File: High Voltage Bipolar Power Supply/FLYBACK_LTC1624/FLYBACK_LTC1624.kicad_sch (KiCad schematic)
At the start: 0 parts

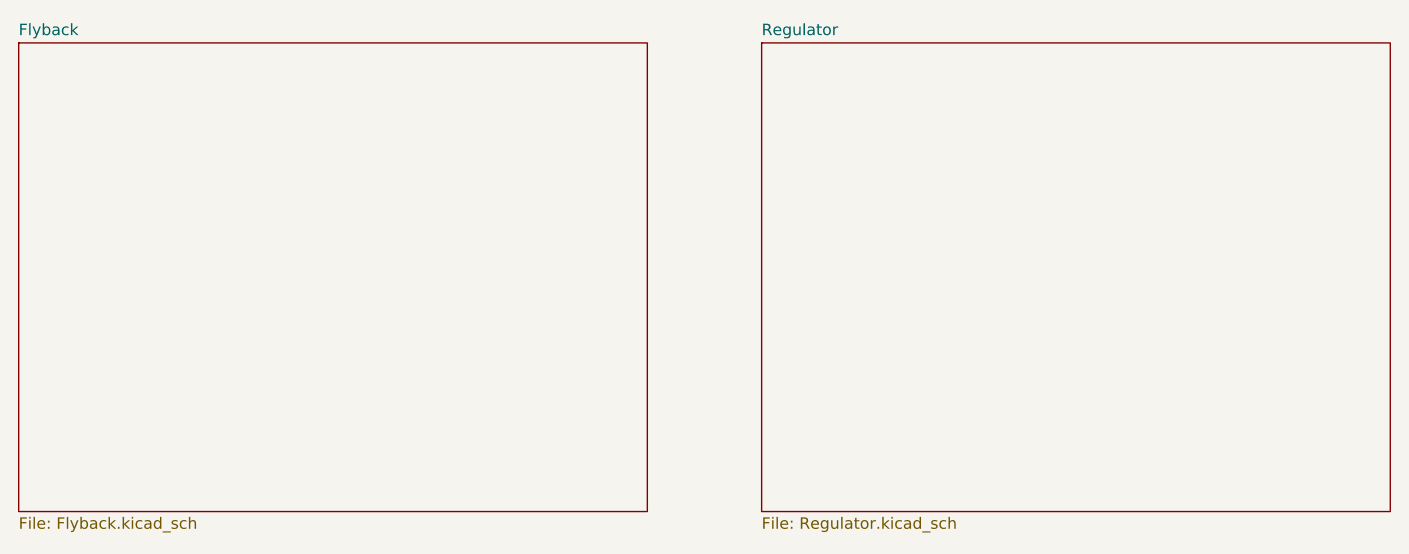
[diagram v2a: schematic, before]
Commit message: FLYBACK_LTC1624: PCB layout
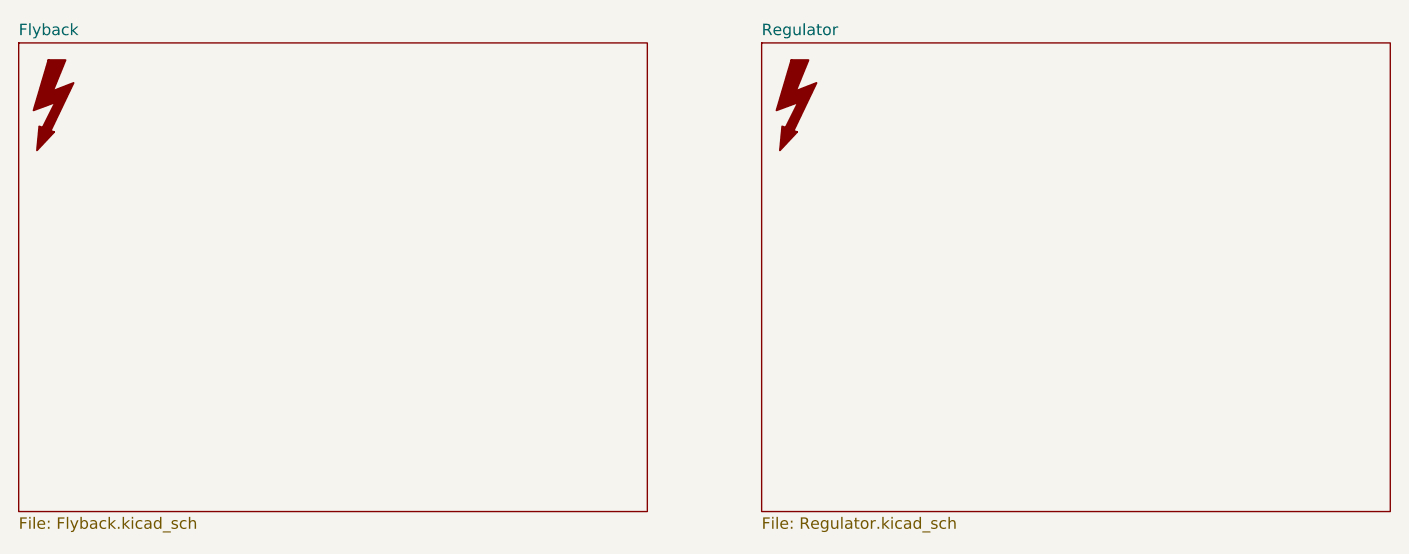
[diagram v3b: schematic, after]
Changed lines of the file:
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@@
 	(generator_version "8.0")
 	(paper "A4")
+	(symbol
+		(lib_id "Graphic:SYM_Flash_Large")
+		(at 149.86 69.85 0)
+		(unit 1)
+		(exclude_from_sim yes)
+		(in_bom no)
+		(on_board no)
+		(dnp no)
+		(fields_autoplaced yes)
+		(property "Reference" "#SYM2"
+			(at 146.05 69.85 90)
+			(effects
+				(font
+					(size 1.27 1.27)
+				)
+				(hide yes)
+			)
+		)
+		(property "Value" "SYM_Flash_Large"
+			(at 153.162 69.85 90)
+			(effects
+				(font
+					(size 1.27 1.27)
+				)
+				(hide yes)
+			)
+		)
+		(property "Footprint" ""
+			(at 149.606 72.136 0)
+			(effects
+				(font
+					(size 1.27 1.27)
+				)
+				(hide yes)
+			)
+		)
+		(property "Datasheet" "~"
+			(at 160.02 72.39 0)
+			(effects
+				(font
+					(size 1.27 1.27)
+				)
+				(hide yes)
+			)
+		)
+		(property "Description" "Flash symbol, large"
+			(at 149.86 69.85 0)
+			(effects
+				(font
+					(size 1.27 1.27)
+				)
+				(hide yes)
+			)
+		)
+		(instances
+			(project "FLYBACK_LTC1624"
+				(path "/b6dc4b50-1aef-431e-aae5-8ba2077040d1"
+					(reference "#SYM2")
+					(unit 1)
+				)
+			)
+		)
+	)
+	(symbol
+		(lib_id "Graphic:SYM_Flash_Large")
+		(at 67.31 69.85 0)
+		(unit 1)
+		(exclude_from_sim no)
+		(in_bom no)
+		(on_board no)
+		(dnp no)
+		(fields_autoplaced yes)
+		(property "Reference" "#SYM1"
+			(at 63.5 69.85 90)
+			(effects
+				(font
+					(size 1.27 1.27)
+				)
+				(hide yes)
+			)
+		)
+		(property "Value" "SYM_Flash_Large"
+			(at 70.612 69.85 90)
+			(effects
+				(font
+					(size 1.27 1.27)
+				)
+				(hide yes)
+			)
+		)
+		(property "Footprint" ""
+			(at 67.056 72.136 0)
+			(effects
+				(font
+					(size 1.27 1.27)
+				)
+				(hide yes)
+			)
+		)
+		(property "Datasheet" "~"
+			(at 77.47 72.39 0)
+			(effects
+				(font
+					(size 1.27 1.27)
+				)
+				(hide yes)
+			)
+		)
+		(property "Description" "Flash symbol, large"
+			(at 67.31 69.85 0)
+			(effects
+				(font
+					(size 1.27 1.27)
+				)
+				(hide yes)
+			)
+		)
+		(property "Sim.Enable" "0"
+			(at 67.31 69.85 0)
+			(effects
+				(font
+					(size 1.27 1.27)
+				)
+				(hide yes)
+			)
+		)
+		(instances
+			(project ""
+				(path "/b6dc4b50-1aef-431e-aae5-8ba2077040d1"
+					(reference "#SYM1")
+					(unit 1)
+				)
+			)
+		)
+	)
 	(sheet
 		(at 63.5 63.5)
@@
 		)
 		(fill
-			(color 0 0 0 0.0000)
+			(color 255 255 194 1.0000)
 		)
 		(property "Sheetname" "Flyback"
@@
 		)
 		(fill
-			(color 0 0 0 0.0000)
+			(color 255 255 194 1.0000)
 		)
 		(property "Sheetname" "Regulator"

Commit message: FLYBACK_LTC1624 : Design failed, can't buy LM377HV for -50V
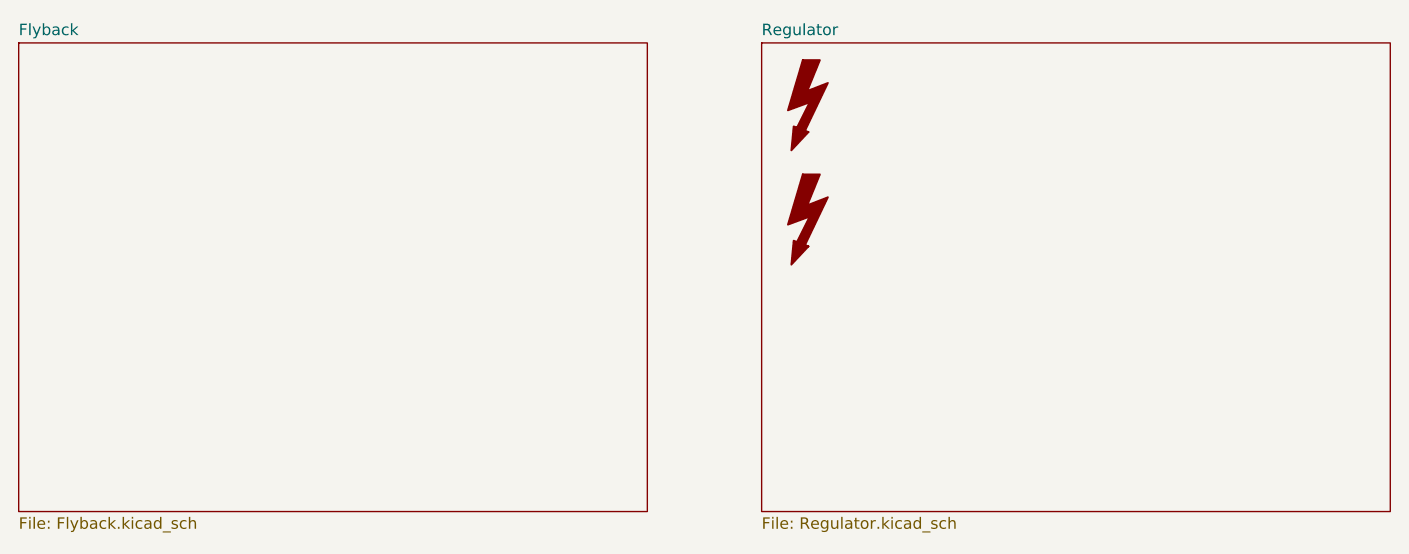
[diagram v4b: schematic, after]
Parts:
- added SYM1: SYM_Flash_Large, Symbol:Symbol_Attention_Triangle_8x7mm_Copper, symbol Graphic:SYM_Flash_Large
- added SYM2: SYM_Flash_Large, Symbol:Symbol_HighVoltage_Triangle_8x7mm_Copper, symbol Graphic:SYM_Flash_Large
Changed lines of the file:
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@@
 	(symbol
 		(lib_id "Graphic:SYM_Flash_Large")
-		(at 149.86 69.85 0)
+		(at 151.13 69.85 0)
 		(unit 1)
 		(exclude_from_sim yes)
 		(in_bom no)
-		(on_board no)
+		(on_board yes)
 		(dnp no)
 		(fields_autoplaced yes)
-		(property "Reference" "#SYM2"
-			(at 146.05 69.85 90)
+		(property "Reference" "SYM2"
+			(at 147.32 69.85 90)
 			(effects
 				(font
@@
 		)
 		(property "Value" "SYM_Flash_Large"
-			(at 153.162 69.85 90)
+			(at 154.432 69.85 90)
 			(effects
 				(font
@@
 			)
 		)
-		(property "Footprint" ""
-			(at 149.606 72.136 0)
+		(property "Footprint" "Symbol:Symbol_HighVoltage_Triangle_8x7mm_Copper"
+			(at 150.876 72.136 0)
 			(effects
 				(font
@@
 		)
 		(property "Datasheet" "~"
-			(at 160.02 72.39 0)
+			(at 161.29 72.39 0)
 			(effects
 				(font
@@
 		)
 		(property "Description" "Flash symbol, large"
-			(at 149.86 69.85 0)
+			(at 151.13 69.85 0)
 			(effects
 				(font
@@
 			(project "FLYBACK_LTC1624"
 				(path "/b6dc4b50-1aef-431e-aae5-8ba2077040d1"
-					(reference "#SYM2")
+					(reference "SYM2")
 					(unit 1)
 				)
@@
 	(symbol
 		(lib_id "Graphic:SYM_Flash_Large")
-		(at 67.31 69.85 0)
+		(at 151.13 82.55 0)
 		(unit 1)
-		(exclude_from_sim no)
+		(exclude_from_sim yes)
 		(in_bom no)
-		(on_board no)
+		(on_board yes)
 		(dnp no)
 		(fields_autoplaced yes)
-		(property "Reference" "#SYM1"
-			(at 63.5 69.85 90)
+		(property "Reference" "SYM1"
+			(at 147.32 82.55 90)
 			(effects
 				(font
@@
 		)
 		(property "Value" "SYM_Flash_Large"
-			(at 70.612 69.85 90)
+			(at 154.432 82.55 90)
 			(effects
 				(font
@@
 			)
 		)
-		(property "Footprint" ""
-			(at 67.056 72.136 0)
+		(property "Footprint" "Symbol:Symbol_Attention_Triangle_8x7mm_Copper"
+			(at 150.876 84.836 0)
 			(effects
 				(font
@@
 		)
 		(property "Datasheet" "~"
-			(at 77.47 72.39 0)
+			(at 161.29 85.09 0)
 			(effects
 				(font
@@
 		)
 		(property "Description" "Flash symbol, large"
-			(at 67.31 69.85 0)
-			(effects
-				(font
-					(size 1.27 1.27)
-				)
-				(hide yes)
-			)
-		)
-		(property "Sim.Enable" "0"
-			(at 67.31 69.85 0)
+			(at 151.13 82.55 0)
 			(effects
 				(font
@@
 		)
 		(instances
-			(project ""
+			(project "FLYBACK_LTC1624"
 				(path "/b6dc4b50-1aef-431e-aae5-8ba2077040d1"
-					(reference "#SYM1")
+					(reference "SYM1")
 					(unit 1)
 				)
